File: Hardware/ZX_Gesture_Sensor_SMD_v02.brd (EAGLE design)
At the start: 57.3 x 19.1 mm, 51 parts, among them Q1 MMBT2222A, Q2 MOSFET-NCHANNEL2N7002PW, U1 PIC16F1823-14PINTSSOP, U2 MCP6021T-E/OT, U3 DMC2700UDM, U4 DMC2700UDM, U6 TSOP57238TT1

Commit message: Updated Board and Schematic Files
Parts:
- JP3: value (none) -> Note: use 1x3 male headers (CONN-009692)
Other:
- board text added: "v02"
- board text removed: "v10"
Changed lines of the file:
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@@
 <text x="28.6639" y="8.2804" size="0.8128" layer="22" font="vector" ratio="15" rot="MR180" align="bottom-center">I2C Addr</text>
 <text x="25.0444" y="17.3355" size="1.27" layer="21" font="vector" ratio="15" align="bottom-center">ZX Gesture</text>
-<text x="53.1495" y="14.9225" size="1.2192" layer="1" font="vector" ratio="15" rot="R135" align="center">v10</text>
+<text x="53.1495" y="14.9225" size="1.2192" layer="1" font="vector" ratio="15" rot="R135" align="center">v02</text>
 <text x="47.6885" y="2.667" size="0.8128" layer="22" font="vector" ratio="15" rot="MR0" align="bottom-center">I2C Pullups</text>
 <text x="18.4785" y="2.3495" size="0.8128" layer="21" font="vector" ratio="15" align="bottom-center">GRN</text>
@@
 <element name="U6" library="SparkFun-Sensors" package="TSOP572" value="TSOP57238TT1" x="28.575" y="9.525" rot="R180">
 <attribute name="PROD_ID" value="COMP-11990" x="13.335" y="42.545" size="1.778" layer="27" rot="R180" display="off"/>
-<attribute name="PLACE" value="DNP" x="28.575" y="9.525" size="1.778" layer="27" rot="R180" display="off"/>
 </element>
 <element name="JP1" library="SparkFun-Connectors" package="1X06_NO_SILK" value="" x="18.415" y="1.27">
 <attribute name="PROD_ID" value="CONN-08437" x="18.415" y="1.27" size="1.778" layer="27" display="off"/>
 </element>
-<element name="JP3" library="SparkFun-Connectors" package="1X03_NO_SILK" value="" x="33.655" y="1.27"/>
+<element name="JP3" library="SparkFun-Connectors" package="1X03_NO_SILK" value="Note: use 1x3 male headers (CONN-009692)" x="33.655" y="1.27"/>
 <element name="R1" library="SparkFun-Resistors" package="0603-RES" value="100k" x="22.225" y="15.24" rot="MR90">
 <attribute name="PROD_ID" value="RES-07828" x="-26.035" y="30.48" size="1.778" layer="28" rot="MR90" display="off"/>

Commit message: Updated Board and schematic files
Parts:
- renumbered D3 to D1, D4 to D2
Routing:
- net N$12: track 19.3 -> 0.00 mm, vias 1 -> 0
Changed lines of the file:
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@@
 <setting verticaltext="up"/>
 </settings>
-<grid distance="0.00625" unitdist="inch" unit="inch" style="dots" multiple="1" display="yes" altdistance="0.005" altunitdist="inch" altunit="inch"/>
+<grid distance="0.05" unitdist="inch" unit="inch" style="dots" multiple="1" display="yes" altdistance="0.005" altunitdist="inch" altunit="inch"/>
 <layers>
 <layer number="1" name="Top" color="4" fill="1" visible="yes" active="yes"/>
@@
 <layer number="19" name="Unrouted" color="6" fill="1" visible="yes" active="yes"/>
 <layer number="20" name="Dimension" color="15" fill="1" visible="yes" active="yes"/>
-<layer number="21" name="tPlace" color="16" fill="1" visible="no" active="yes"/>
+<layer number="21" name="tPlace" color="16" fill="1" visible="yes" active="yes"/>
 <layer number="22" name="bPlace" color="14" fill="1" visible="yes" active="yes"/>
 <layer number="23" name="tOrigins" color="15" fill="1" visible="yes" active="yes"/>
@@
 <element name="TP5" library="SparkFun-Passives" package="PAD.03X.04" value="TEST-POINT3X4" x="33.9725" y="5.715" rot="MR0"/>
 <element name="U$6" library="SparkFun-Aesthetics" package="GESTURESENSE_TEXT" value="GESTURESENSE_LOGOSTEXT" x="32.512" y="6.096"/>
-<element name="D3" library="SparkFun-LED" package="SFH4641-SHORT2" value="SFH4641SHORT2" x="9.525" y="9.525" rot="R270">
+<element name="D1" library="SparkFun-LED" package="SFH4641-SHORT2" value="SFH4641SHORT2" x="9.525" y="9.525" rot="R270">
 <attribute name="PROD_ID" value="DIO-11994" x="9.525" y="9.525" size="1.778" layer="27" font="vector" ratio="15" rot="R270" display="off"/>
 </element>
-<element name="D4" library="SparkFun-LED" package="SFH4641-SHORT2" value="SFH4641SHORT2" x="47.625" y="9.525" rot="R90">
+<element name="D2" library="SparkFun-LED" package="SFH4641-SHORT2" value="SFH4641SHORT2" x="47.625" y="9.525" rot="R90">
 <attribute name="PROD_ID" value="DIO-11994" x="47.625" y="9.525" size="1.778" layer="27" font="vector" ratio="15" rot="R90" display="off"/>
 </element>
@@
 <contactref element="C4" pad="1"/>
 <contactref element="C6" pad="1"/>
-<contactref element="D3" pad="C"/>
-<contactref element="D4" pad="C"/>
+<contactref element="D1" pad="C"/>
+<contactref element="D2" pad="C"/>
 <wire x1="14.14" y1="17.145" x2="14.2875" y2="17.2925" width="0.2032" layer="16"/>
 <via x="45.085" y="17.4625" extent="1-16" drill="0.381"/>
@@
 <signal name="N$7">
 <contactref element="R6" pad="2"/>
-<contactref element="D3" pad="A"/>
+<contactref element="D1" pad="A"/>
 <wire x1="9.945" y1="15.5575" x2="9.945" y2="15.3425" width="0.254" layer="16"/>
 <wire x1="9.945" y1="15.3425" x2="9.8425" y2="15.24" width="0.254" layer="16"/>
@@
 <wire x1="45.4025" y1="8.8225" x2="46.7425" y2="10.1625" width="0.2032" layer="16"/>
 </signal>
-<signal name="N$12">
-<contactref element="R8" pad="2"/>
-<contactref element="D4" pad="A"/>
-<wire x1="45.4025" y1="10.375" x2="43.395" y2="10.375" width="0.508" layer="16"/>
-<wire x1="43.395" y1="10.375" x2="43.18" y2="10.16" width="0.508" layer="16"/>
-<via x="43.18" y="10.16" extent="1-16" drill="0.381"/>
-<wire x1="43.18" y1="10.16" x2="43.18" y2="5.08" width="0.508" layer="1"/>
-<wire x1="43.18" y1="5.08" x2="44.45" y2="3.81" width="0.508" layer="1"/>
-<wire x1="44.45" y1="3.81" x2="48.26" y2="3.81" width="0.508" layer="1"/>
-<wire x1="48.26" y1="3.81" x2="49.66" y2="5.21" width="0.508" layer="1"/>
-<wire x1="49.66" y1="9.525" x2="49.66" y2="5.21" width="0.508" layer="1"/>
-</signal>
 <signal name="RECEIVER">
 <contactref element="U6" pad="1"/>
@@
 <signal name="N$25">
 </signal>
+<signal name="N$12">
+<contactref element="D2" pad="A"/>
+<contactref element="R8" pad="2"/>
+<wire x1="45.4025" y1="10.375" x2="49.66" y2="9.525" width="0" layer="19" extent="1-16"/>
+</signal>
 </signals>

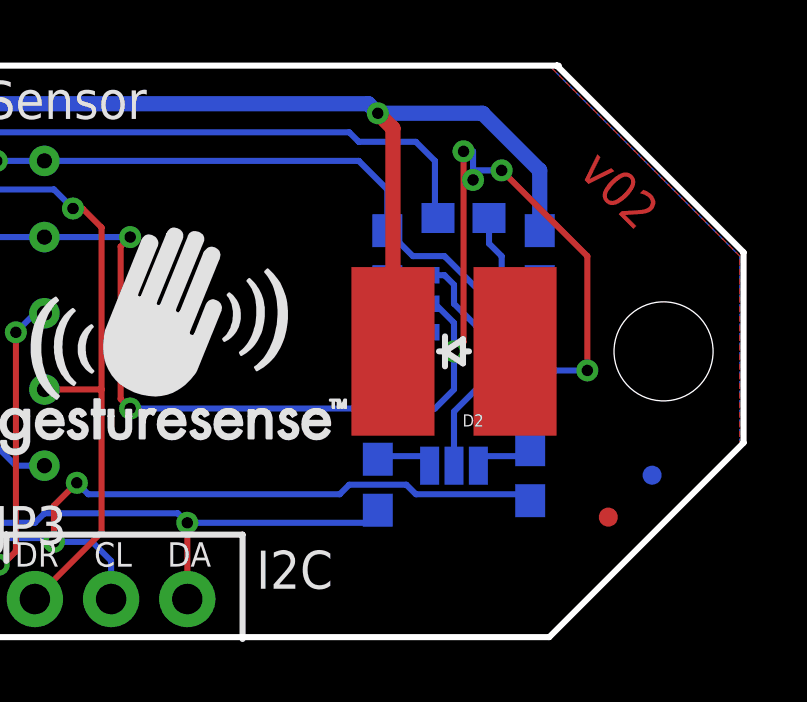
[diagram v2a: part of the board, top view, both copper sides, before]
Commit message: Updated Board and Schematic per QC
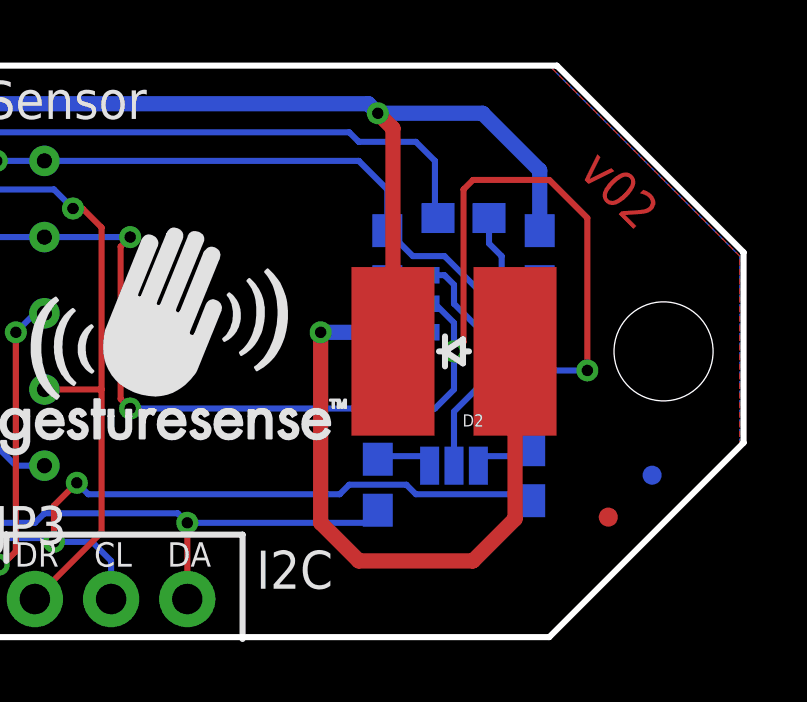
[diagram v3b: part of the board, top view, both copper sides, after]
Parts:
- JP3: value Note: use 1x3 male headers (CONN-009692) -> (none)
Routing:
- net N$12: track 0.00 -> 21.8 mm, vias 0 -> 1
- net GND: track 129.7 -> 128.2 mm, vias 17 -> 14
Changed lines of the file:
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@@
 <dimension x1="54.61" y1="9.525" x2="57.15" y2="9.525" x3="55.88" y3="-11.1125" textsize="1.778" textratio="15" layer="47" unit="inch"/>
 <wire x1="6.35" y1="19.05" x2="51.054" y2="19.05" width="0.2032" layer="20"/>
-<wire x1="51.054" y1="19.05" x2="51.1175" y2="19.05" width="0.2032" layer="20"/>
 <wire x1="51.054" y1="19.05" x2="57.277" y2="12.827" width="0.2032" layer="20"/>
 <wire x1="57.277" y1="12.827" x2="57.277" y2="6.477" width="0.2032" layer="20"/>
@@
 <attribute name="PROD_ID" value="CONN-08437" x="18.415" y="1.27" size="1.778" layer="27" display="off"/>
 </element>
-<element name="JP3" library="SparkFun-Connectors" package="1X03_NO_SILK" value="Note: use 1x3 male headers (CONN-009692)" x="33.655" y="1.27"/>
+<element name="JP3" library="SparkFun-Connectors" package="1X03_NO_SILK" value="" x="33.655" y="1.27"/>
 <element name="R1" library="SparkFun-Resistors" package="0603-RES" value="100k" x="22.225" y="15.24" rot="MR90">
 <attribute name="PROD_ID" value="RES-07828" x="-26.035" y="30.48" size="1.778" layer="28" rot="MR90" display="off"/>
@@
 <wire x1="7.3025" y1="12.8025" x2="8.54" y2="12.8025" width="0.2032" layer="16"/>
 <wire x1="8.54" y1="12.8025" x2="8.6425" y2="12.7" width="0.2032" layer="16"/>
-<wire x1="49.1425" y1="11.1125" x2="49.8475" y2="11.1125" width="0.2032" layer="16"/>
+<wire x1="49.1425" y1="11.1125" x2="50.1015" y2="11.1125" width="0.2032" layer="16"/>
 <wire x1="48.895" y1="11.1125" x2="47.3075" y2="12.7" width="0.2032" layer="16"/>
 <wire x1="48.895" y1="11.1125" x2="49.1425" y2="11.1125" width="0.2032" layer="16"/>
 <wire x1="50.165" y1="11.43" x2="50.4825" y2="11.43" width="0.2032" layer="16"/>
-<wire x1="49.8475" y1="11.1125" x2="50.165" y2="11.43" width="0.2032" layer="16"/>
 <wire x1="50.4825" y1="10.375" x2="50.4825" y2="10.4775" width="0.2032" layer="16"/>
-<wire x1="50.4825" y1="10.4775" x2="49.8475" y2="11.1125" width="0.2032" layer="16"/>
 <wire x1="47.3075" y1="12.7" x2="46.2525" y2="12.7" width="0.2032" layer="16"/>
 <wire x1="46.2525" y1="12.7" x2="45.4025" y2="13.55" width="0.2032" layer="16"/>
@@
 <wire x1="26.9875" y1="15.875" x2="26.9875" y2="17.4625" width="0.2032" layer="1"/>
 <wire x1="26.9875" y1="17.4625" x2="27.305" y2="17.78" width="0.2032" layer="1"/>
+<wire x1="50.165" y1="11.43" x2="50.165" y2="11.049" width="0.2032" layer="16"/>
+<wire x1="50.165" y1="11.049" x2="50.165" y2="10.6925" width="0.2032" layer="16"/>
+<wire x1="50.165" y1="10.6925" x2="50.4825" y2="10.375" width="0.2032" layer="16"/>
+<wire x1="50.1015" y1="11.1125" x2="50.165" y2="11.049" width="0.2032" layer="16"/>
 </signal>
 <signal name="GND">
@@
 <vertex x="0" y="6.35"/>
 </polygon>
-<via x="48.26" y="15.24" extent="1-16" drill="0.381"/>
 <wire x1="18.7325" y1="15.9051" x2="18.7325" y2="15.24" width="0.2032" layer="16"/>
 <wire x1="18.7325" y1="15.24" x2="18.415" y2="14.9225" width="0.2032" layer="16"/>
@@
 <wire x1="20.955" y1="14.9225" x2="18.415" y2="14.9225" width="0.2032" layer="16"/>
 <wire x1="20.955" y1="14.39" x2="20.955" y2="14.9225" width="0.2032" layer="16"/>
-<wire x1="48.26" y1="16.1925" x2="48.26" y2="15.5575" width="0.2032" layer="16"/>
-<wire x1="47.9425" y1="16.1925" x2="48.26" y2="16.1925" width="0.2032" layer="16"/>
-<wire x1="47.9425" y1="9.8425" x2="47.9425" y2="16.1925" width="0.2032" layer="1"/>
+<wire x1="47.9425" y1="9.8425" x2="47.9425" y2="14.9225" width="0.2032" layer="1"/>
 <wire x1="47.625" y1="9.525" x2="47.9425" y2="9.8425" width="0.2032" layer="1"/>
 <wire x1="47.625" y1="10.4775" x2="47.625" y2="9.525" width="0.2032" layer="16"/>
 <wire x1="46.99" y1="11.1125" x2="47.625" y2="10.4775" width="0.2032" layer="16"/>
 <wire x1="46.99" y1="11.1125" x2="46.7425" y2="11.1125" width="0.2032" layer="16"/>
-<via x="47.9425" y="16.1925" extent="1-16" drill="0.381"/>
 <via x="47.625" y="9.525" extent="1-16" drill="0.381"/>
 <wire x1="52.07" y1="8.89" x2="50.4825" y2="8.89" width="0.2032" layer="16"/>
-<wire x1="52.07" y1="12.7" x2="52.07" y2="8.89" width="0.2032" layer="1"/>
-<wire x1="49.2125" y1="15.5575" x2="52.07" y2="12.7" width="0.2032" layer="1"/>
-<wire x1="48.26" y1="15.5575" x2="49.2125" y2="15.5575" width="0.2032" layer="16"/>
+<wire x1="52.07" y1="13.97" x2="52.07" y2="8.89" width="0.2032" layer="1"/>
 <wire x1="50.4825" y1="8.89" x2="50.4825" y2="8.675" width="0.2032" layer="16"/>
-<wire x1="48.26" y1="15.5575" x2="48.26" y2="15.24" width="0.2032" layer="16"/>
 <via x="52.07" y="8.89" extent="1-16" drill="0.381"/>
-<via x="49.2125" y="15.5575" extent="1-16" drill="0.381"/>
 <wire x1="47.625" y1="8.255" x2="47.625" y2="9.525" width="0.2032" layer="16"/>
 <wire x1="46.99" y1="7.62" x2="47.625" y2="8.255" width="0.2032" layer="16"/>
@@
 <wire x1="22.905" y1="12.81375" x2="22.70125" y2="13.0175" width="0.2032" layer="16"/>
 <wire x1="22.70125" y1="13.0175" x2="21.2725" y2="13.0175" width="0.2032" layer="16"/>
+<wire x1="47.9425" y1="14.9225" x2="48.26" y2="15.24" width="0.2032" layer="1"/>
+<wire x1="48.26" y1="15.24" x2="50.8" y2="15.24" width="0.2032" layer="1"/>
+<wire x1="50.8" y1="15.24" x2="52.07" y2="13.97" width="0.2032" layer="1"/>
 </signal>
 <signal name="I2C_SDA">
@@
 <contactref element="D2" pad="A"/>
 <contactref element="R8" pad="2"/>
-<wire x1="45.4025" y1="10.375" x2="49.66" y2="9.525" width="0" layer="19" extent="1-16"/>
+<via x="43.18" y="10.16" extent="1-16" drill="0.381"/>
+<wire x1="49.66" y1="9.525" x2="49.66" y2="3.94" width="0.508" layer="1"/>
+<wire x1="49.66" y1="3.94" x2="48.26" y2="2.54" width="0.508" layer="1"/>
+<wire x1="48.26" y1="2.54" x2="44.45" y2="2.54" width="0.508" layer="1"/>
+<wire x1="44.45" y1="2.54" x2="43.18" y2="3.81" width="0.508" layer="1"/>
+<wire x1="43.18" y1="3.81" x2="43.18" y2="10.16" width="0.508" layer="1"/>
+<wire x1="43.18" y1="10.16" x2="45.1875" y2="10.16" width="0.508" layer="16"/>
+<wire x1="45.1875" y1="10.16" x2="45.4025" y2="10.375" width="0.2032" layer="16"/>
 </signal>
 </signals>
+<errors>
+</errors>
 </board>
 </drawing>

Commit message: Updated Board Files per QC
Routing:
- net VCC: track 106.9 -> 106.3 mm
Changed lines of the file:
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@@
 <wire x1="23.241" y1="6.9215" x2="23.241" y2="6.7065" width="0.2032" layer="16"/>
 <wire x1="23.241" y1="6.7065" x2="24.13" y2="5.8175" width="0.2032" layer="16"/>
-<wire x1="29.3425" y1="6.0325" x2="29.3425" y2="5.265" width="0.2032" layer="16"/>
-<wire x1="29.3425" y1="5.265" x2="29.5275" y2="5.08" width="0.2032" layer="16"/>
-<wire x1="29.5275" y1="5.08" x2="30.5825" y2="5.08" width="0.2032" layer="16"/>
-<wire x1="30.5825" y1="5.08" x2="30.7975" y2="4.865" width="0.2032" layer="16"/>
 <wire x1="27.305" y1="15.5575" x2="27.305" y2="12.3825" width="0.2032" layer="1"/>
 <wire x1="26.9875" y1="15.875" x2="27.305" y2="15.5575" width="0.2032" layer="1"/>
@@
 <wire x1="24.13" y1="5.715" x2="24.13" y2="5.8175" width="0.2032" layer="16"/>
 <via x="25.7175" y="5.715" extent="1-16" drill="0.381"/>
-<wire x1="29.21" y1="5.08" x2="29.21" y2="5.3975" width="0.2032" layer="16"/>
-<wire x1="29.5275" y1="5.08" x2="29.21" y2="5.08" width="0.2032" layer="16"/>
-<wire x1="30.7975" y1="4.7625" x2="32.0675" y2="4.7625" width="0.2032" layer="16"/>
 <wire x1="30.7975" y1="4.7625" x2="30.7975" y2="4.865" width="0.2032" layer="16"/>
-<wire x1="32.0675" y1="5.08" x2="32.0675" y2="4.7625" width="0.2032" layer="16"/>
 <wire x1="32.385" y1="5.3975" x2="32.0675" y2="5.08" width="0.2032" layer="1"/>
 <wire x1="32.385" y1="9.8425" x2="32.385" y2="5.3975" width="0.2032" layer="1"/>
@@
 <wire x1="50.165" y1="10.6925" x2="50.4825" y2="10.375" width="0.2032" layer="16"/>
 <wire x1="50.1015" y1="11.1125" x2="50.165" y2="11.049" width="0.2032" layer="16"/>
+<wire x1="29.3425" y1="6.0325" x2="29.3425" y2="5.0745" width="0.2032" layer="16"/>
+<wire x1="29.3425" y1="5.0745" x2="29.718" y2="4.699" width="0.2032" layer="16"/>
+<wire x1="29.718" y1="4.699" x2="30.6315" y2="4.699" width="0.2032" layer="16"/>
+<wire x1="30.6315" y1="4.699" x2="30.7975" y2="4.865" width="0.2032" layer="16"/>
+<wire x1="30.7975" y1="4.7625" x2="31.75" y2="4.7625" width="0.2032" layer="16"/>
+<wire x1="31.75" y1="4.7625" x2="32.0675" y2="5.08" width="0.2032" layer="16"/>
 </signal>
 <signal name="GND">

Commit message: Updated Brd File
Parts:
- moved FRAME1 14.0 mm to (-4.76, -8.57)
- moved LOGO1 14.0 mm to (26.4, -14.9)
- moved U$5 2.17 mm to (13.3, 6.95)
- moved U$6 0.40 mm to (32.1, 6.22)
- moved U1 0.13 mm to (21.0, 8.45)
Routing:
- net GND: track 128.2 -> 128.3 mm, vias 14 -> 16
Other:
- board size 57.3 x 19.1 mm -> 57.2 x 19.1 mm

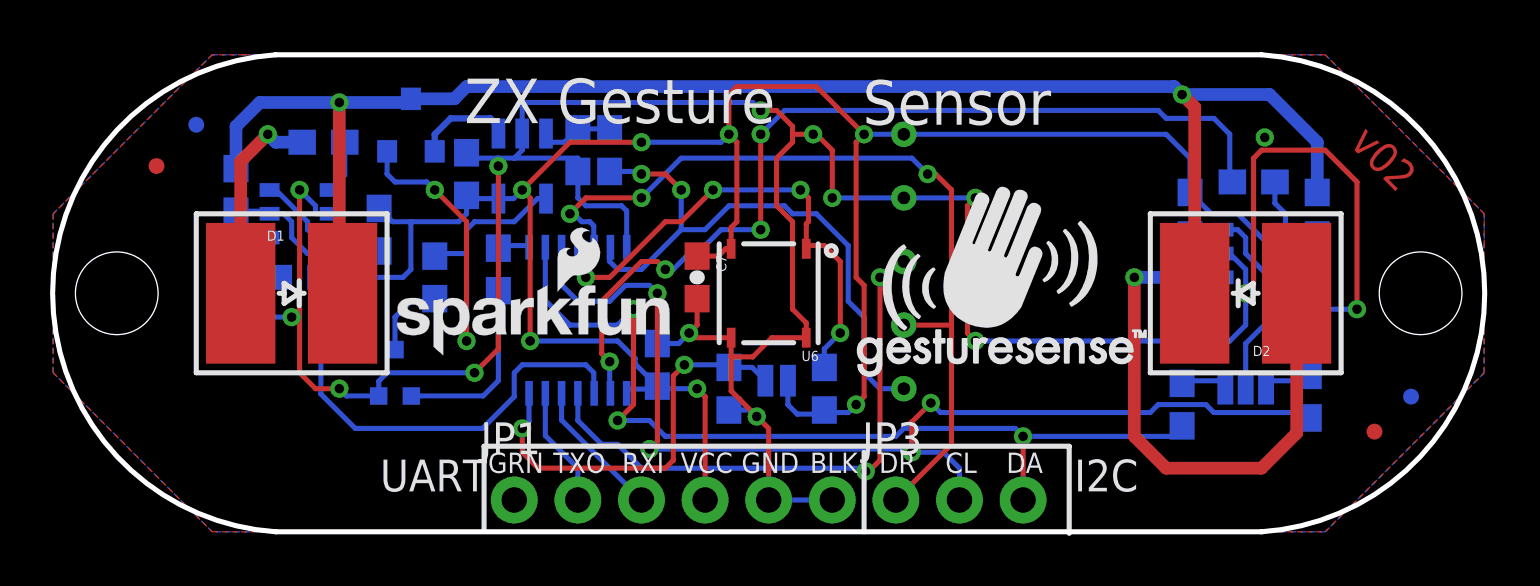
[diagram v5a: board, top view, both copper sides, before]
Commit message: Moved Programming Pins
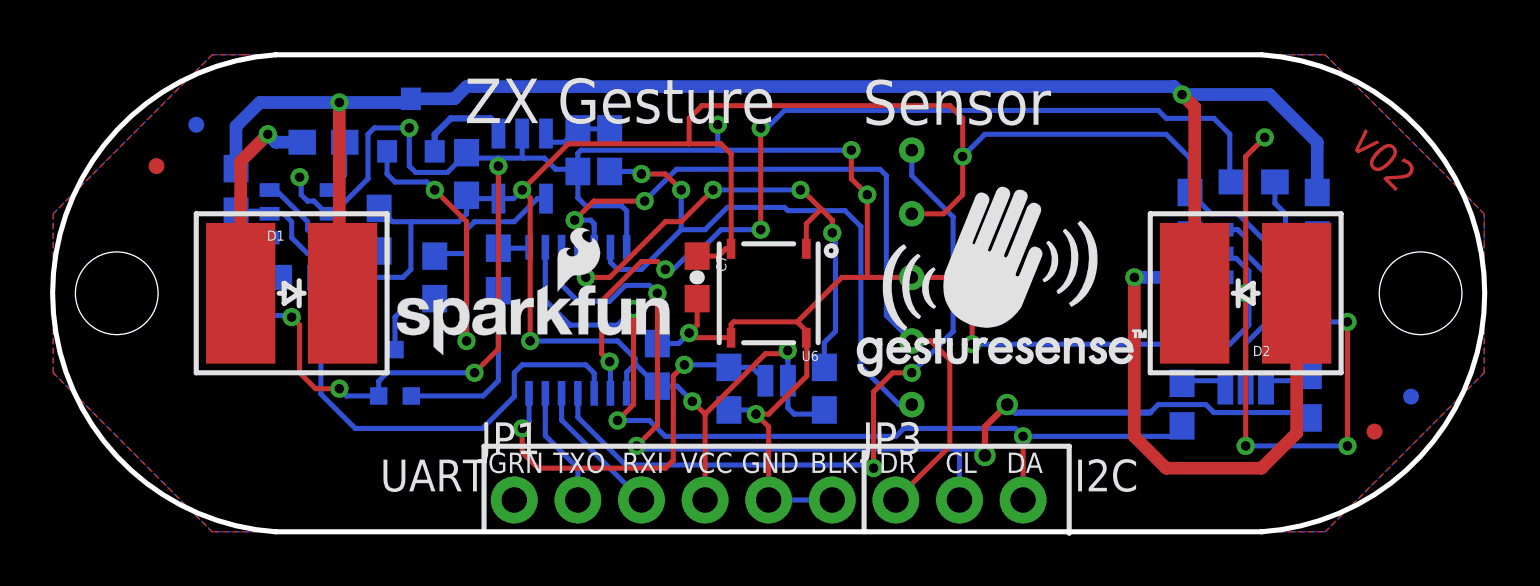
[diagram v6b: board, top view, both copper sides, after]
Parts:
- moved U$1 8.58 mm to (43.9, 6.48), turned to 0 degrees
- moved TP3 4.46 mm to (34.3, 15.2)
- moved TP1 3.19 mm to (34.3, 12.7)
- moved TP2 3.19 mm to (34.3, 10.2)
- moved TP4 0.71 mm to (34.3, 7.62)
- moved TP5 0.71 mm to (34.3, 5.08)
- moved LOGO2 0.64 mm to (8.19, 3.37)
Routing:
- net MCLR: track 22.7 -> 28.8 mm
- net ICSPCLK/DATA_RDY: track 33.9 -> 30.5 mm, vias 4 -> 3
- net GND: track 128.3 -> 131.2 mm, vias 16 -> 18
- net VCC: track 106.4 -> 104.1 mm, vias 8 -> 6
- net RECEIVER: track 20.0 -> 21.1 mm
- net ICSPDAT/DACOUT: track 24.1 -> 25.1 mm
- net I2C_SCL: track 44.4 -> 43.5 mm
